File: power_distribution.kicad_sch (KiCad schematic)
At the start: 83 parts, among them Q1 PMOS, Q10 2PNP, Q11 2NPN, Q12 PMOS, Q13 2PNP, Q14 2PNP, Q15 2PNP, Q2 PMOS, Q3 2NPN, Q4 PMOS, Q5 PMOS, Q6 PMOS, Q7 PMOS, Q8 2NPN, Q9 PMOS, U1 PAC1954

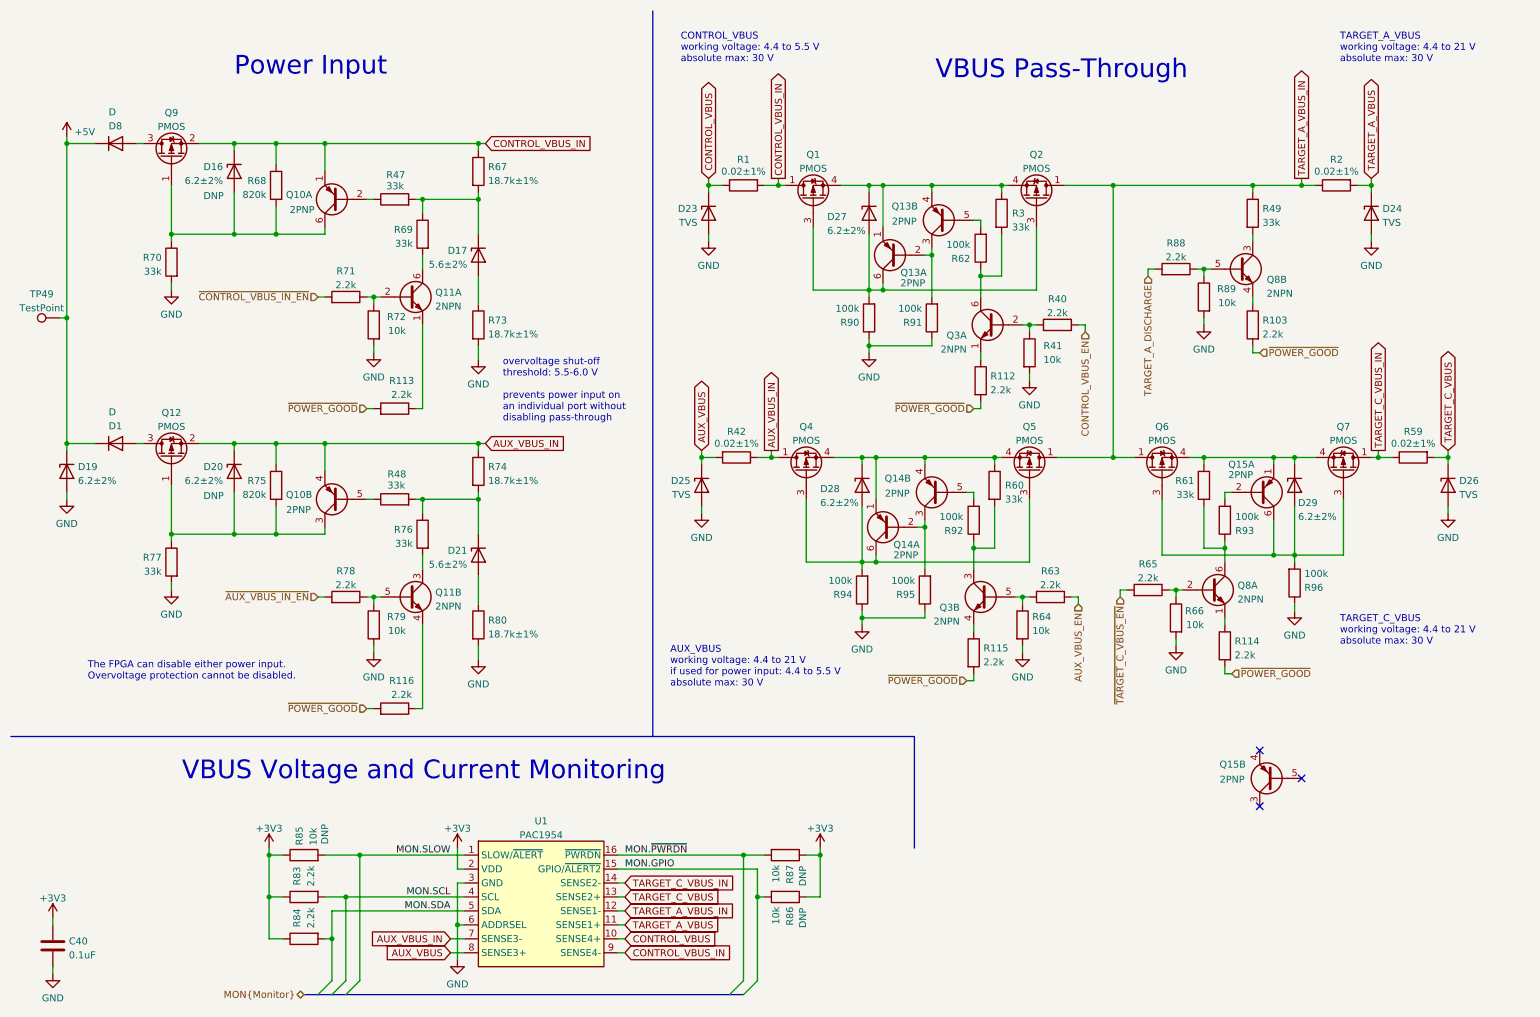
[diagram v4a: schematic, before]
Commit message: Use four-terminal current sense resistor symbol
Previously we had used a special four-terminal symbol and footprint to
ensure that current sense signals did not connect to power supply zones
in multiple places. We rejected this in favor of a two-terminal
schematic symbol and standard resistor footprint to ensure reliable
assembly.

This new solution uses a four-terminal schematic symbol with a
two-terminal footprint which is actually four terminals in two
overlapping pairs using the "net tie" footprint feature.

Fixes #13
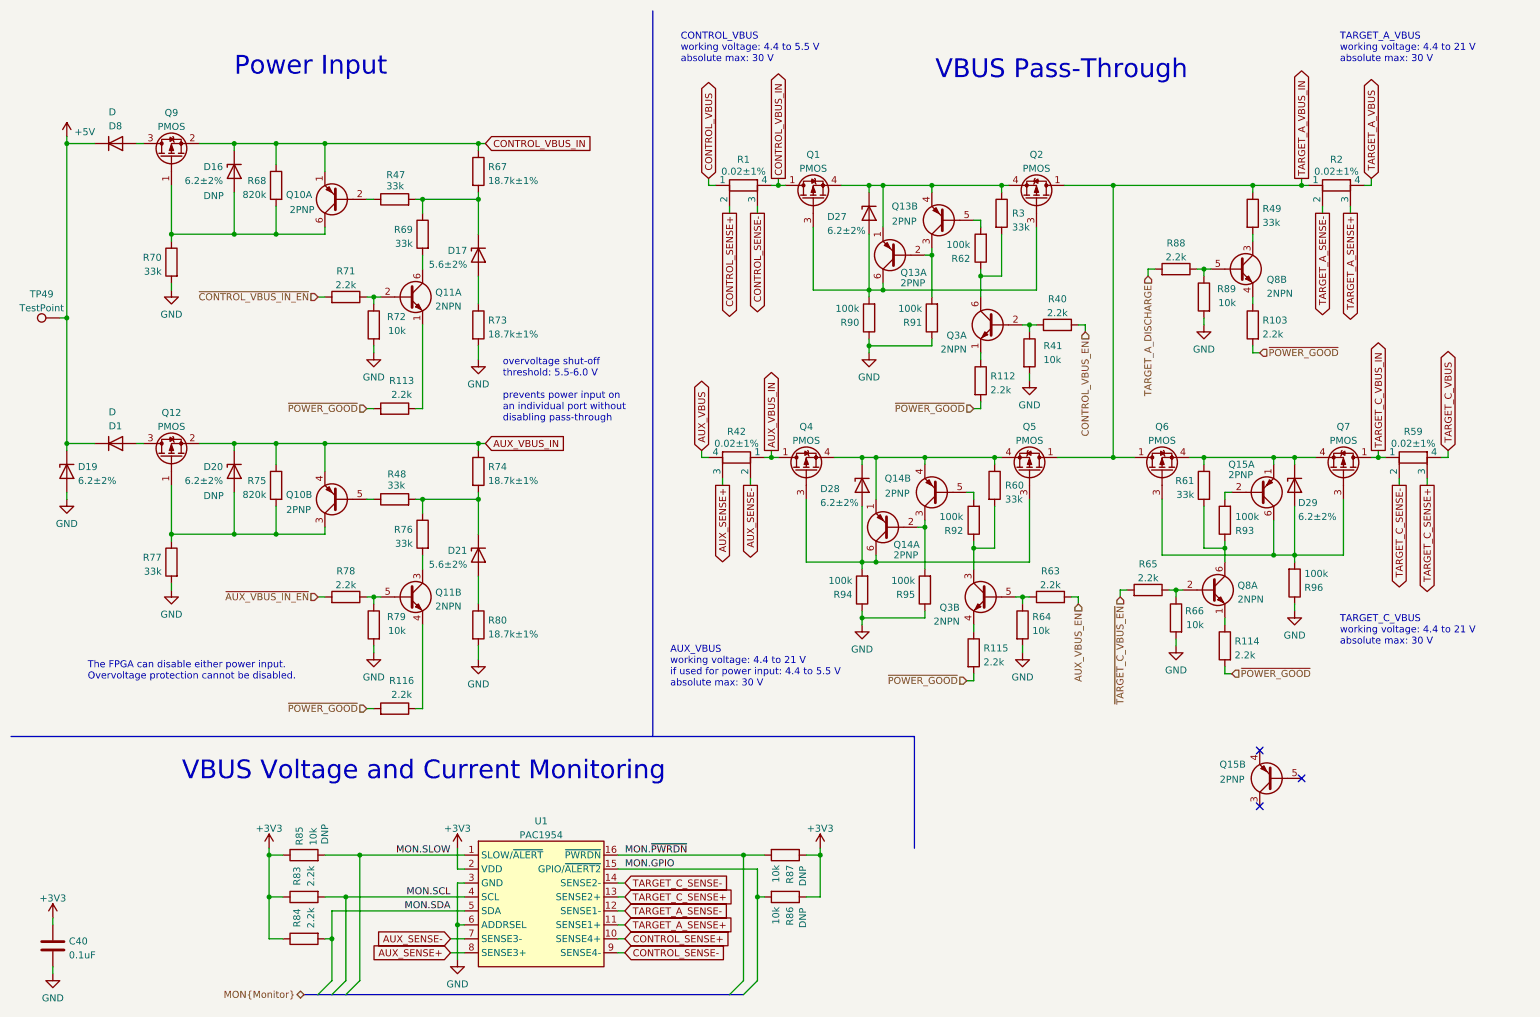
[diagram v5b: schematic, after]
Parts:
- removed D23, D24, D25, D26: TVS, cynthion:DFN1006-2, symbol Device:D_Zener
- R1, R2, R42, R59: footprint Resistor_SMD:R_0603_1608Metric -> cynthion:R_0603_1608Metric_Current_Sense; symbol Device:R -> Device:R_Shunt
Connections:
- net AUX_VBUS: now also R42.4; no longer R42.2, U1.8 (SENSE3+)
- net AUX_VBUS_IN: no longer U1.7 (SENSE3-)
- net CONTROL_VBUS: no longer U1.10 (SENSE4+)
- net CONTROL_VBUS_IN: now also R1.4; no longer R1.2, U1.9 (SENSE4-)
- net TARGET_A_VBUS: now also R2.4; no longer R2.2, U1.11 (SENSE1+)
- net TARGET_A_VBUS_IN: no longer U1.12 (SENSE1-)
- net TARGET_C_VBUS: now also R59.4; no longer R59.2, U1.13 (SENSE2+)
- net TARGET_C_VBUS_IN: no longer U1.14 (SENSE2-)
- new net AUX_SENSE+: R42.3, U1.8 (SENSE3+)
- new net AUX_SENSE-: R42.2, U1.7 (SENSE3-)
- new net CONTROL_SENSE+: R1.2, U1.10 (SENSE4+)
- new net CONTROL_SENSE-: R1.3, U1.9 (SENSE4-)
- new net TARGET_A_SENSE+: R2.3, U1.11 (SENSE1+)
- new net TARGET_A_SENSE-: R2.2, U1.12 (SENSE1-)
- new net TARGET_C_SENSE+: R59.3, U1.13 (SENSE2+)
- new net TARGET_C_SENSE-: R59.2, U1.14 (SENSE2-)

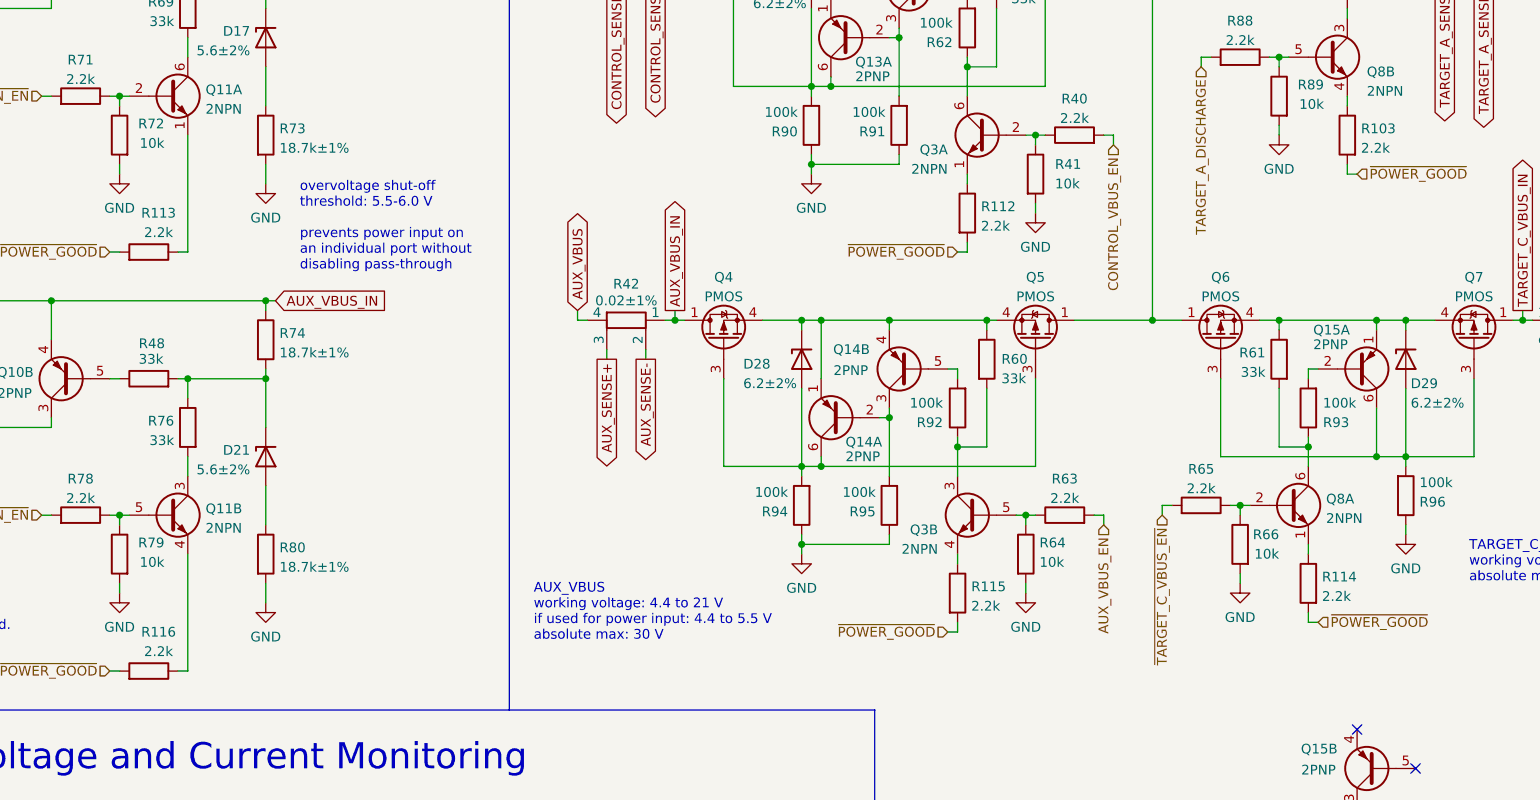
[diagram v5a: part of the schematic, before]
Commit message: Replace POWER_GOOD series resistors with 0 ohms
Fixes #15
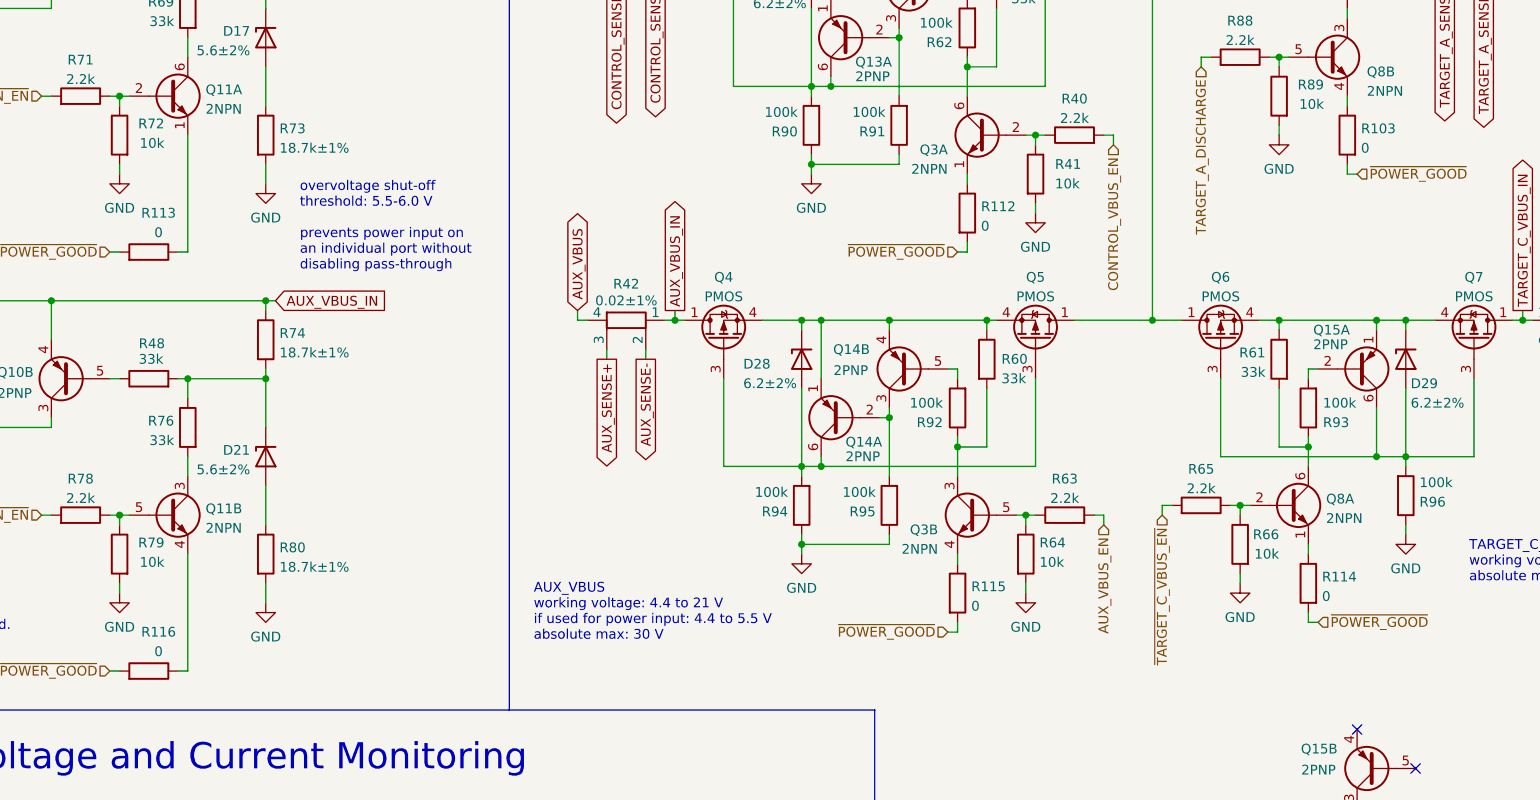
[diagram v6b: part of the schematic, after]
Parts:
- R103, R112, R113, R114, R115, R116: value 2.2k -> 0; Part Number RC0402JR-072K2L -> RC0402FR-070RL
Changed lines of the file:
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@@
       (effects (font (size 1.27 1.27)))
     )
-    (property "Value" "2.2k" (at 83.82 82.55 90)
+    (property "Value" "0" (at 83.82 82.55 90)
       (effects (font (size 1.27 1.27)))
     )
@@
       (effects (font (size 1.27 1.27)) hide)
     )
-    (property "Part Number" "RC0402JR-072K2L" (at 82.55 85.09 0)
+    (property "Part Number" "RC0402FR-070RL" (at 82.55 85.09 0)
       (effects (font (size 1.27 1.27)) hide)
     )
@@
       (effects (font (size 1.27 1.27)) hide)
     )
-    (property "Description" "RES 2.2K OHM 5% 1/16W 0402" (at 82.55 85.09 0)
+    (property "Description" "RES 0 OHM JUMPER 1/16W 0402" (at 82.55 85.09 0)
       (effects (font (size 1.27 1.27)) hide)
     )
@@
       (effects (font (size 1.27 1.27)) (justify right))
     )
-    (property "Value" "2.2k" (at 235.458 129.9722 0)
+    (property "Value" "0" (at 235.458 129.9722 0)
       (effects (font (size 1.27 1.27)) (justify right))
     )
@@
       (effects (font (size 1.27 1.27)) hide)
     )
-    (property "Part Number" "RC0402JR-072K2L" (at 233.68 128.27 0)
+    (property "Part Number" "RC0402FR-070RL" (at 233.68 128.27 0)
       (effects (font (size 1.27 1.27)) hide)
     )
@@
       (effects (font (size 1.27 1.27)) hide)
     )
-    (property "Description" "RES 2.2K OHM 5% 1/16W 0402" (at 233.68 128.27 0)
+    (property "Description" "RES 0 OHM JUMPER 1/16W 0402" (at 233.68 128.27 0)
       (effects (font (size 1.27 1.27)) hide)
     )
@@
       (effects (font (size 1.27 1.27)) (justify right))
     )
-    (property "Value" "2.2k" (at 240.538 71.5522 0)
+    (property "Value" "0" (at 240.538 71.5522 0)
       (effects (font (size 1.27 1.27)) (justify right))
     )
@@
       (effects (font (size 1.27 1.27)) hide)
     )
-    (property "Part Number" "RC0402JR-072K2L" (at 238.76 69.85 0)
+    (property "Part Number" "RC0402FR-070RL" (at 238.76 69.85 0)
       (effects (font (size 1.27 1.27)) hide)
     )
@@
       (effects (font (size 1.27 1.27)) hide)
     )
-    (property "Description" "RES 2.2K OHM 5% 1/16W 0402" (at 238.76 69.85 0)
+    (property "Description" "RES 0 OHM JUMPER 1/16W 0402" (at 238.76 69.85 0)
       (effects (font (size 1.27 1.27)) hide)
     )
@@
       (effects (font (size 1.27 1.27)) (justify left))
     )
-    (property "Value" "2.2k" (at 189.738 131.2422 0)
+    (property "Value" "0" (at 189.738 131.2422 0)
       (effects (font (size 1.27 1.27)) (justify left))
     )
@@
       (effects (font (size 1.27 1.27)) hide)
     )
-    (property "Part Number" "RC0402JR-072K2L" (at 187.96 129.54 0)
+    (property "Part Number" "RC0402FR-070RL" (at 187.96 129.54 0)
       (effects (font (size 1.27 1.27)) hide)
     )
@@
       (effects (font (size 1.27 1.27)) hide)
     )
-    (property "Description" "RES 2.2K OHM 5% 1/16W 0402" (at 187.96 129.54 0)
+    (property "Description" "RES 0 OHM JUMPER 1/16W 0402" (at 187.96 129.54 0)
       (effects (font (size 1.27 1.27)) hide)
     )
@@
       (effects (font (size 1.27 1.27)) (justify left))
     )
-    (property "Value" "2.2k" (at 191.008 81.7122 0)
+    (property "Value" "0" (at 191.008 81.7122 0)
       (effects (font (size 1.27 1.27)) (justify left))
     )
@@
       (effects (font (size 1.27 1.27)) hide)
     )
-    (property "Part Number" "RC0402JR-072K2L" (at 189.23 80.01 0)
+    (property "Part Number" "RC0402FR-070RL" (at 189.23 80.01 0)
       (effects (font (size 1.27 1.27)) hide)
     )
@@
       (effects (font (size 1.27 1.27)) hide)
     )
-    (property "Description" "RES 2.2K OHM 5% 1/16W 0402" (at 189.23 80.01 0)
+    (property "Description" "RES 0 OHM JUMPER 1/16W 0402" (at 189.23 80.01 0)
       (effects (font (size 1.27 1.27)) hide)
     )
@@
       (effects (font (size 1.27 1.27)))
     )
-    (property "Value" "2.2k" (at 83.82 137.16 90)
+    (property "Value" "0" (at 83.82 137.16 90)
       (effects (font (size 1.27 1.27)))
     )
@@
       (effects (font (size 1.27 1.27)) hide)
     )
-    (property "Part Number" "RC0402JR-072K2L" (at 82.55 139.7 0)
+    (property "Part Number" "RC0402FR-070RL" (at 82.55 139.7 0)
       (effects (font (size 1.27 1.27)) hide)
     )
@@
       (effects (font (size 1.27 1.27)) hide)
     )
-    (property "Description" "RES 2.2K OHM 5% 1/16W 0402" (at 82.55 139.7 0)
-      (effects (font (size 1.27 1.27)) hide)
-    )
+    (property "Description" "RES 0 OHM JUMPER 1/16W 0402" (at 82.55 139.7 0)
+      (effects (font (size 1.27 1.27)) hide)
+    )

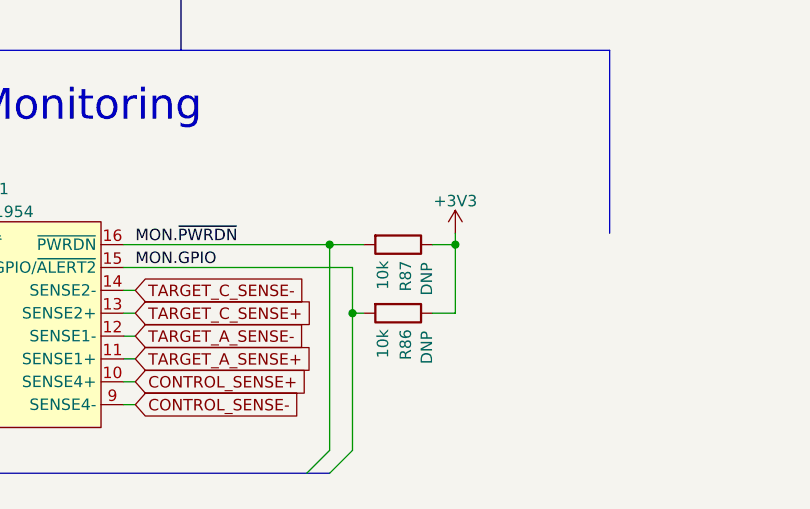
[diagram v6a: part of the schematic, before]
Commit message: Power up U1 PAC1954 by default
Previously it was (probably but not guaranteed to be) powered down until
after FPGA configuration, but it is potentially useful to have it start
collecting measurement data immediately when the board powers on.
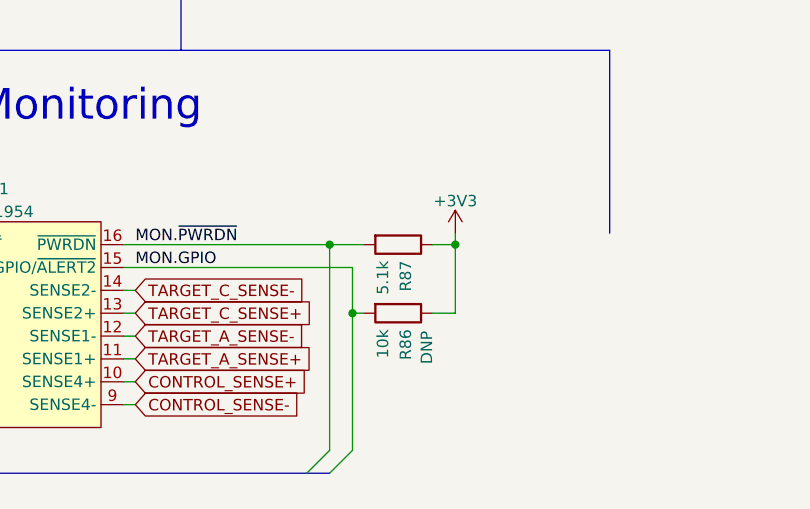
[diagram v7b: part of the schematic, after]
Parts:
- R87: value 10k -> 5.1k; DNP DNP -> (none); Part Number RC0402JR-0710KL -> RC0402JR-075K1L
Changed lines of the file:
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@@
       (effects (font (size 1.27 1.27)) (justify left))
     )
-    (property "Value" "10k" (at 151.9678 168.148 0)
+    (property "Value" "5.1k" (at 151.9678 168.148 0)
       (effects (font (size 1.27 1.27)) (justify left))
     )
@@
       (effects (font (size 1.27 1.27)) hide)
     )
-    (property "Part Number" "RC0402JR-0710KL" (at 153.67 166.37 0)
+    (property "Part Number" "RC0402JR-075K1L" (at 153.67 166.37 0)
       (effects (font (size 1.27 1.27)) hide)
     )
@@
       (effects (font (size 1.27 1.27)) hide)
     )
-    (property "Description" "RES 10K OHM 5% 1/16W 0402" (at 153.67 166.37 0)
+    (property "Description" "RES 5.1K OHM 5% 1/16W 0402" (at 153.67 166.37 0)
       (effects (font (size 1.27 1.27)) hide)
     )
@@
       (effects (font (size 1.27 1.27)) hide)
     )
-    (property "DNP" "DNP" (at 156.845 170.18 0)
-      (effects (font (size 1.27 1.27)))
-    )
     (pin "1")
